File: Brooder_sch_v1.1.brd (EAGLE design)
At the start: 80 x 75 mm, 25 parts, among them J1 DCJ0202, J2 1X2-3.5MM, U1 328P

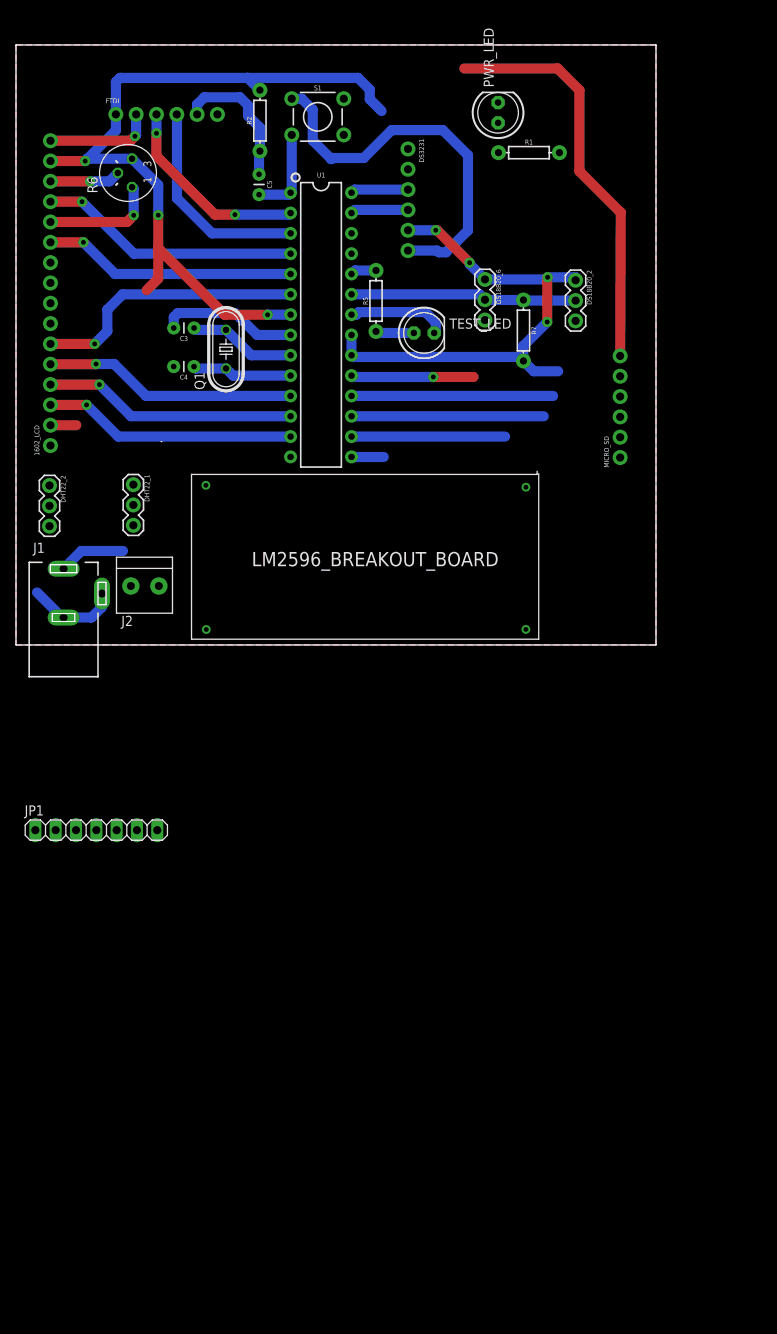
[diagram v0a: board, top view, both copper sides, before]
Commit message: Adds the sim800 to the PCB board
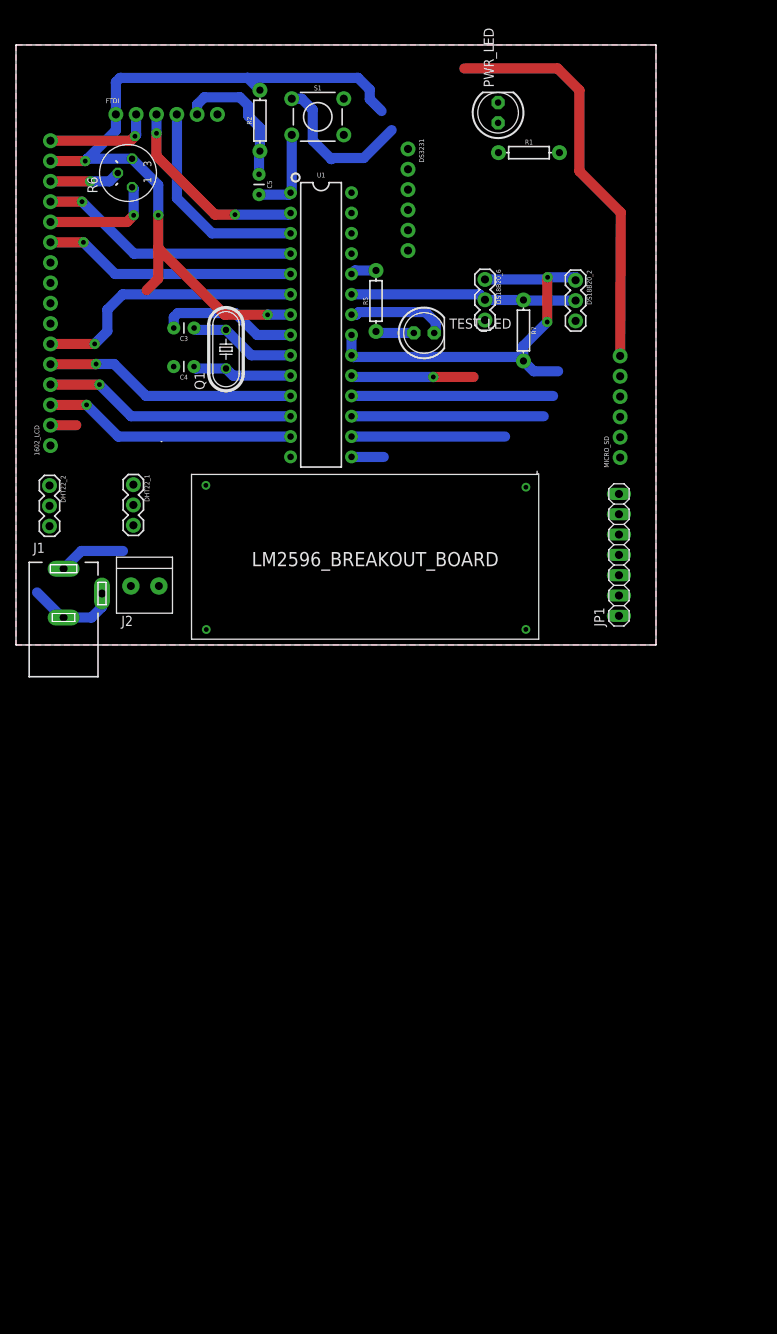
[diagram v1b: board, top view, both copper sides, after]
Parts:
- moved JP1 73.8 mm to (75.4, 11.3), turned to 90 degrees
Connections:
- removed net N$12: JP1.7
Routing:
- net GND: track 168.7 -> 139.7 mm
- net 5V: track 166.9 -> 154.6 mm, vias 7 -> 5
- net PC5: track 7.22 -> 0.00 mm
- net PC4: track 7.22 -> 0.00 mm
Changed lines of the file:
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@@
 </element>
 <element name="U$2" library="LM2596_BREAKOUT_BOARD" package="LM2596_BREAKOUTBOARD" value="" x="65.24" y="21.42" rot="R180"/>
-<element name="JP1" library="pinhead" package="1X07" value="" x="10.04" y="-23.15"/>
+<element name="JP1" library="pinhead" package="1X07" value="" x="75.37" y="11.26" rot="R90"/>
 </elements>
 <signals>
@@
 <wire x1="42.86" y1="41.61" x2="51.18" y2="41.61" width="1.27" layer="16"/>
 <wire x1="51.18" y1="41.61" x2="52.47" y2="40.32" width="1.27" layer="16"/>
-<wire x1="49" y1="49.3" x2="52.64" y2="49.3" width="1.27" layer="16"/>
-<wire x1="52.64" y1="49.3" x2="52.86" y2="49.08" width="1.27" layer="16"/>
-<wire x1="52.86" y1="49.08" x2="53.76" y2="49.08" width="1.27" layer="16"/>
-<wire x1="56.5" y1="51.82" x2="56.5" y2="61.21" width="1.27" layer="16"/>
-<wire x1="56.5" y1="61.21" x2="53.35" y2="64.36" width="1.27" layer="16"/>
 <wire x1="39.57" y1="60.87" x2="39.43" y2="60.73" width="1.27" layer="16"/>
 <wire x1="39.43" y1="60.73" x2="39.42" y2="60.73" width="1.27" layer="16"/>
@@
 <wire x1="37.09" y1="66.9" x2="35.7094" y2="68.2806" width="1.27" layer="16"/>
 <wire x1="35.7094" y1="68.2806" x2="34.4688" y2="68.2806" width="1.27" layer="16"/>
-<wire x1="53.76" y1="49.08" x2="56.5" y2="51.82" width="1.27" layer="16"/>
-<wire x1="53.35" y1="64.36" x2="46.96" y2="64.36" width="1.27" layer="16"/>
 <wire x1="46.96" y1="64.36" x2="43.47" y2="60.87" width="1.27" layer="16"/>
 <wire x1="43.47" y1="60.87" x2="39.57" y2="60.87" width="1.27" layer="16"/>
@@
 <wire x1="56.04" y1="72.06" x2="60.26" y2="67.8" width="0" layer="19" extent="1-1"/>
 <wire x1="69.95" y1="40.51" x2="75.52" y2="36.13" width="0" layer="19" extent="1-1"/>
-<wire x1="56.5" y1="61.21" x2="60.26" y2="67.8" width="0" layer="19" extent="16-16"/>
-<wire x1="51.18" y1="41.61" x2="52.86" y2="49.08" width="0" layer="19" extent="16-16"/>
-<wire x1="58.62" y1="40.61" x2="52.47" y2="40.32" width="0" layer="19" extent="16-16"/>
+<wire x1="58.62" y1="40.61" x2="69.95" y2="40.51" width="0" layer="19" extent="1-1"/>
+<wire x1="52.47" y1="40.32" x2="58.62" y2="40.61" width="0" layer="19" extent="16-16"/>
+<wire x1="49" y1="49.3" x2="51.18" y2="41.61" width="0" layer="19" extent="16-16"/>
 <wire x1="34.32" y1="38.75" x2="41.94" y2="41.29" width="0" layer="19" extent="1-1"/>
 <wire x1="19.71" y1="34.8" x2="19.72" y2="39.62" width="0" layer="19" extent="1-1"/>
+<wire x1="46.96" y1="64.36" x2="56.04" y2="72.06" width="0" layer="19" extent="1-16"/>
 <wire x1="13.87" y1="52.87" x2="20.24" y2="41.49" width="0" layer="19" extent="1-16"/>
 <wire x1="14.31" y1="63.03" x2="14.508" y2="57.222" width="0" layer="19" extent="1-1"/>
@@
 <wire x1="14.67" y1="14.96" x2="10.75" y2="6.43" width="0" layer="19" extent="1-1"/>
 <wire x1="23.78338125" y1="1.9319125" x2="10.75" y2="4.75" width="0" layer="19" extent="16-16"/>
-<wire x1="15.12" y1="-23.15" x2="23.78338125" y2="1.9319125" width="0" layer="19" extent="1-1"/>
-<wire x1="4.96" y1="-23.15" x2="15.12" y2="-23.15" width="0" layer="19" extent="1-1"/>
-<wire x1="63.735740625" y1="1.945340625" x2="75.52" y2="36.13" width="0" layer="19" extent="1-1"/>
+<wire x1="75.37" y1="16.34" x2="75.52" y2="36.13" width="0" layer="19" extent="1-1"/>
+<wire x1="75.37" y1="6.18" x2="75.37" y2="16.34" width="0" layer="19" extent="1-1"/>
+<wire x1="63.735740625" y1="1.945340625" x2="75.37" y2="6.18" width="0" layer="19" extent="1-1"/>
 </signal>
 <signal name="12V">
@@
 <wire x1="62.93" y1="36" x2="63.43" y2="35.5" width="1.27" layer="16"/>
 <wire x1="42.15" y1="36" x2="62.93" y2="36" width="1.27" layer="16"/>
-<wire x1="52.47" y1="51.84" x2="49" y2="51.84" width="1.27" layer="16"/>
 <wire x1="28.95" y1="70.89" x2="42.75" y2="70.89" width="1.27" layer="16"/>
 <wire x1="44.22" y1="69.42" x2="44.22" y2="68.22" width="1.27" layer="16"/>
@@
 <wire x1="67.77" y1="34.21" x2="64.72" y2="34.21" width="1.27" layer="16"/>
 <wire x1="64.72" y1="34.21" x2="63.43" y2="35.5" width="1.27" layer="16"/>
-<wire x1="58.62" y1="45.69" x2="56.7" y2="47.61" width="1.27" layer="16"/>
-<wire x1="56.7" y1="47.61" x2="56.7" y2="47.78" width="1.27" layer="16"/>
-<via x="56.7" y="47.78" extent="1-16" drill="0.6" diameter="1.3"/>
-<wire x1="56.7" y1="47.78" x2="52.64" y2="51.84" width="1.27" layer="1"/>
-<wire x1="52.64" y1="51.84" x2="52.47" y2="51.84" width="1.27" layer="1"/>
-<via x="52.47" y="51.84" extent="1-16" drill="0.6" diameter="1.3"/>
 <wire x1="17.78" y1="45.8" x2="17.78" y2="49.59" width="1.27" layer="1"/>
 <wire x1="16.33" y1="44.35" x2="17.78" y2="45.8" width="1.27" layer="1"/>
@@
 <wire x1="75.52" y1="33.59" x2="67.77" y2="34.21" width="0" layer="19" extent="16-16"/>
 <wire x1="34.32" y1="41.29" x2="41.94" y2="38.75" width="0" layer="19" extent="1-1"/>
+<wire x1="49" y1="51.84" x2="58.62" y2="45.69" width="0" layer="19" extent="1-1"/>
 <wire x1="63.74" y1="19.72" x2="64.72" y2="34.21" width="0" layer="19" extent="16-16"/>
+<wire x1="75.37" y1="8.72" x2="63.74" y2="19.72" width="0" layer="19" extent="1-1"/>
+<wire x1="75.37" y1="3.64" x2="75.37" y2="8.72" width="0" layer="19" extent="1-1"/>
 <wire x1="7.54" y1="27.47" x2="16.33" y2="44.35" width="0" layer="19" extent="1-1"/>
 <wire x1="4.19" y1="19.93" x2="4.31" y2="27.47" width="0" layer="19" extent="1-1"/>
 <wire x1="14.67" y1="20.04" x2="7.54" y2="27.47" width="0" layer="19" extent="1-1"/>
-<wire x1="2.42" y1="-23.15" x2="4.19" y2="19.93" width="0" layer="19" extent="1-1"/>
-<wire x1="7.5" y1="-23.15" x2="2.42" y2="-23.15" width="0" layer="19" extent="1-1"/>
 </signal>
 <signal name="N$3">
@@
 <contactref element="DS3231" pad="4"/>
 <contactref element="U1" pad="27"/>
-<wire x1="41.94" y1="53.99" x2="42.33" y2="54.38" width="1.27" layer="16"/>
-<wire x1="42.33" y1="54.38" x2="49" y2="54.38" width="1.27" layer="16"/>
+<wire x1="41.94" y1="53.99" x2="49" y2="54.38" width="0" layer="19" extent="1-1"/>
 </signal>
 <signal name="PC5">
 <contactref element="DS3231" pad="3"/>
 <contactref element="U1" pad="28"/>
-<wire x1="41.94" y1="56.53" x2="42.33" y2="56.92" width="1.27" layer="16"/>
-<wire x1="42.33" y1="56.92" x2="49" y2="56.92" width="1.27" layer="16"/>
+<wire x1="41.94" y1="56.53" x2="49" y2="56.92" width="0" layer="19" extent="1-1"/>
 </signal>
 <signal name="TX">
 <contactref element="JP1" pad="4"/>
 <contactref element="U1" pad="25"/>
-<wire x1="10.04" y1="-23.15" x2="41.94" y2="48.91" width="0" layer="19" extent="1-1"/>
+<wire x1="75.37" y1="11.26" x2="41.94" y2="48.91" width="0" layer="19" extent="1-1"/>
 </signal>
 <signal name="RX">
 <contactref element="JP1" pad="5"/>
 <contactref element="U1" pad="26"/>
-<wire x1="12.58" y1="-23.15" x2="41.94" y2="51.45" width="0" layer="19" extent="1-1"/>
-</signal>
-<signal name="N$12">
-<contactref element="JP1" pad="7"/>
+<wire x1="75.37" y1="13.8" x2="41.94" y2="51.45" width="0" layer="19" extent="1-1"/>
 </signal>
 </signals>

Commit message: Adds separate power source for sim800l and board
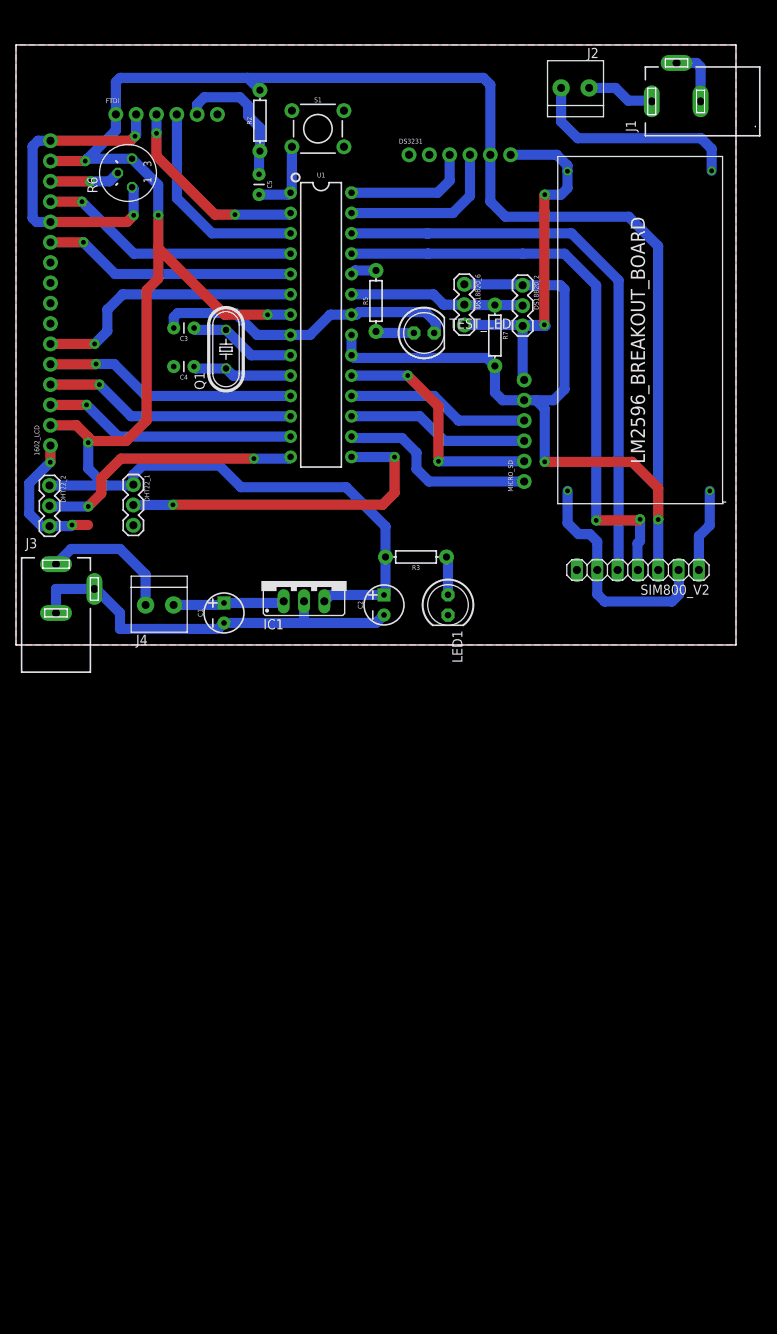
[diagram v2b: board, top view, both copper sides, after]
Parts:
- removed JP1: (no value), pinhead:1X07
- removed PWR_LED: (no value), adafruit:LED5MM
- removed R1: 220, SparkFun-Resistors:AXIAL-0.3
- added C1, C2: 10uF, SparkFun-Capacitors:CPOL-RADIAL-2.5MM-5MM
- added IC1: (no value), v-reg:78XXS
- added J3: DCJ0202, con-jack:DCJ0202
- added J4: 1X2-3.5MM, adafruit:1X2-3.5MM
- added LED1: (no value), adafruit:LED5MM
- added R3: 220, SparkFun-Resistors:AXIAL-0.3
- added SIM800_V2: (no value), pinhead:1X07
- moved J1 98.3 mm to (82.6, 68.0), turned to 90 degrees
- moved J2 82.2 mm to (69.8, 69.6), turned to 0 degrees
- moved U$2 23.5 mm to (88.4, 17.8), turned to 90 degrees
- moved MICRO_SD 12.4 mm to (63.5, 20.4)
- moved DS18B20_2 6.65 mm to (63.3, 45.0)
- moved R7 3.63 mm to (59.9, 38.7)
- moved DS18B20_6 2.65 mm to (56.0, 45.1)
- moved S1 1.49 mm to (37.7, 64.5)
- moved DS3231 0.74 mm to (49.1, 61.3), turned to 0 degrees
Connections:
- removed net N$3: PWR_LED.A, R1.P$1
- new net 12V_SIM: J1.1, J2.1
- new net 12V_S_SIM: J2.2, U$2.IN(+VE)
- new net 5V_SIM: SIM800_V2.1, U$2.OUT(+VE)
- new net N$2: LED1.A, R3.P$1
- net 12V: now also J3.1, J4.1; no longer J1.1, J2.1
- net 12V_S: now also C1.1, IC1.IN, J4.2; no longer J2.2, U$2.IN(+VE)
- net 5V: now also C2.1, IC1.OUT, R3.P$2, SIM800_V2.3; no longer JP1.1, JP1.3, R1.P$2, U$2.OUT(+VE)
- net GND: now also C1.2, C2.2, IC1.GND, J3.2, J3.3, LED1.K, SIM800_V2.2, SIM800_V2.6; no longer JP1.2, JP1.6, PWR_LED.K
- net RX: now also SIM800_V2.5; no longer JP1.5
- net TX: now also SIM800_V2.4; no longer JP1.4
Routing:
- net 5V: track 154.6 -> 376.2 mm, vias 5 -> 6
- net GND: track 139.7 -> 235.6 mm, vias 2 -> 6
- net TX: track 0.00 -> 73.7 mm, vias 0 -> 2
- net RX: track 0.00 -> 72.2 mm
- net PB1: track 4.03 -> 43.1 mm, vias 0 -> 2
- net PB0: track 0.00 -> 33.8 mm, vias 0 -> 2
- net 12V_S_SIM: track 0.00 -> 27.2 mm
- net PC4: track 0.00 -> 20.8 mm
- net PC5: track 0.00 -> 16.1 mm
- net PB5: track 15.3 -> 30.1 mm, vias 1 -> 2
- net 12V_S: track 0.00 -> 14.0 mm
- net 5V_SIM: track 0.00 -> 10.5 mm
- net 12V: track 8.34 -> 17.1 mm
- net 12V_SIM: track 0.00 -> 8.53 mm
- net PC0: track 28.3 -> 22.0 mm
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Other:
- board size 80 x 75 mm -> 90 x 75 mm
